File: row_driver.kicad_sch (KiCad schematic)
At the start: 26 parts, among them SW3 SW_PUSH_SMALL_H, SW4 SW_PUSH_SMALL_H, SW5 SW_PUSH_SMALL_H, SW6 SW_PUSH_SMALL_H, SW7 SW_PUSH_SMALL_H, SW8 SW_PUSH_SMALL_H, U11 74HCT595, U13 74HCT595, U15 74HCT595, U23 CM1293A-04SO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

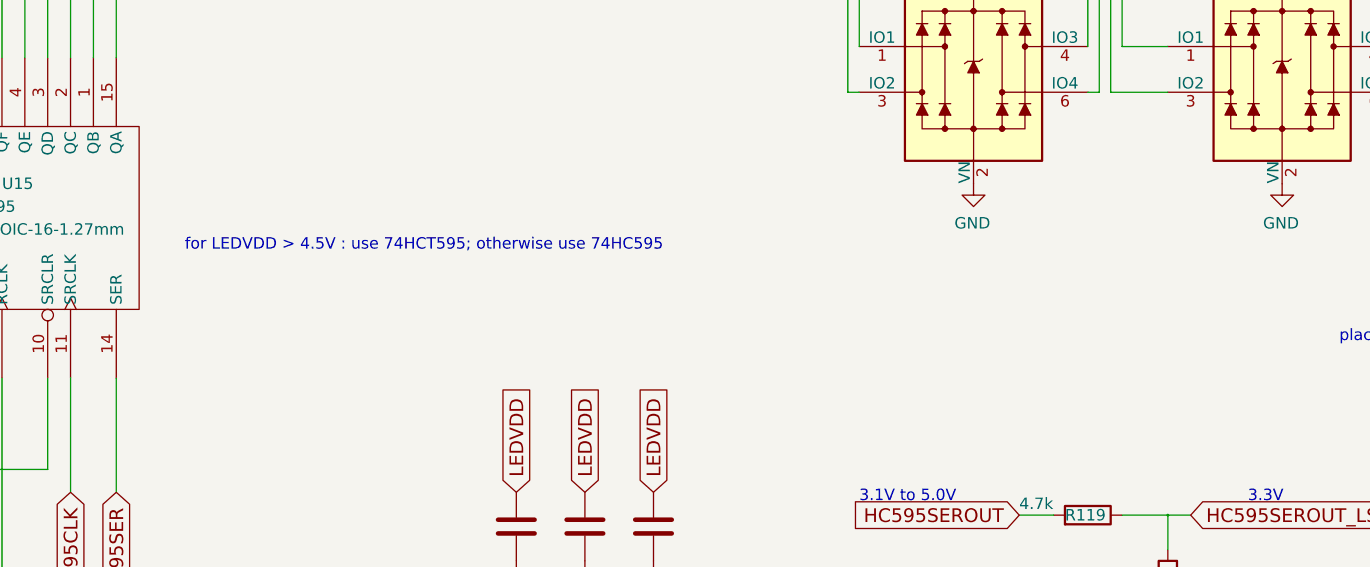
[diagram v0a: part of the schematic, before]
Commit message: Fixed bypass capacitor positions; DRC clear
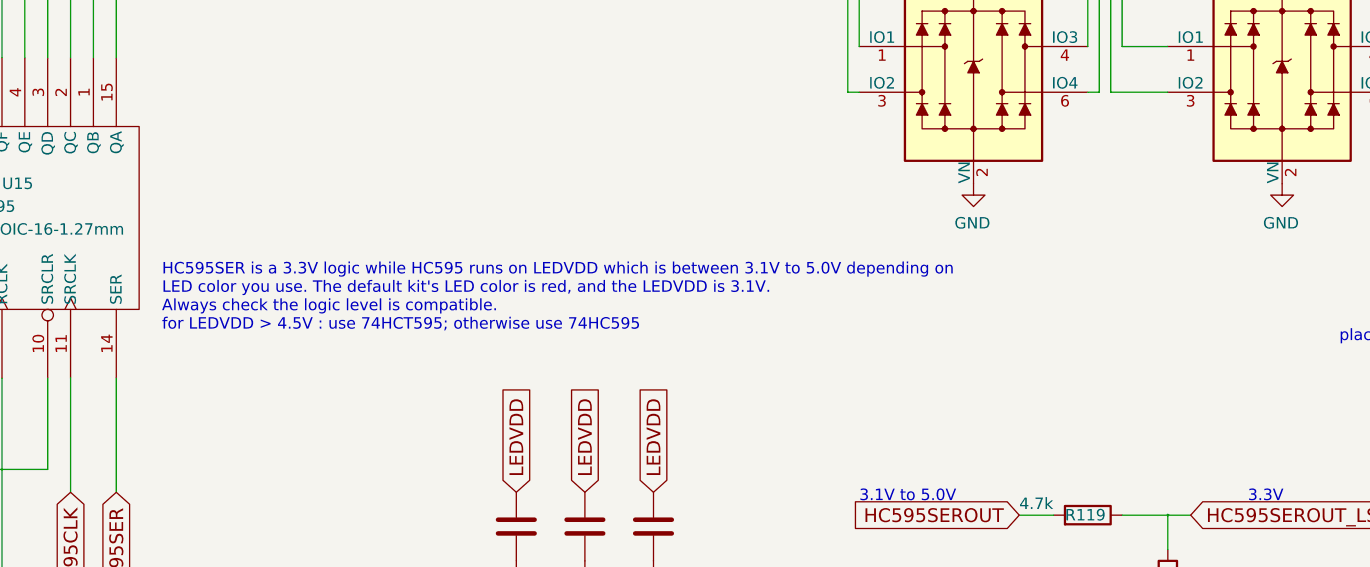
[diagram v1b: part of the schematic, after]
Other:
- note added: "HC595SER is a 3.3V logic while HC595 runs on LEDVDD which is between 3.1V to 5.0V depending on LED color you use. The default kit's LED color is red, and the LEDVDD is 3.1V. Always check the logic level is compatible. for LEDVDD > 4.5V : use 74HCT595; otherwise use 74HC595"
- note removed: "for LEDVDD > 4.5V : use 74HCT595; otherwise use 74HC595"
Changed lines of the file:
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@@
-(kicad_sch (version 20200820) (host eeschema "5.99.0-unknown-dd374e12a~102~ubuntu18.04.1")
+(kicad_sch (version 20200820) (host eeschema "5.99.0-unknown-b0af66afc~103~ubuntu18.04.1")
   (page 4 10)
   (paper "A4")
@@
     (stroke (width 0) (type solid) (color 0 0 0 0))
   )
-  (text "for LEDVDD > 4.5V : use 74HCT595; otherwise use 74HC595"
-    (at 132.08 99.06 0)
+  (text "HC595SER is a 3.3V logic while HC595 runs on LEDVDD which is between 3.1V to 5.0V depending on\nLED color you use. The default kit's LED color is red, and the LEDVDD is 3.1V.\nAlways check the logic level is compatible.\nfor LEDVDD > 4.5V : use 74HCT595; otherwise use 74HC595"
+    (at 129.54 107.95 0)
     (effects (font (size 1.27 1.27)) (justify left bottom))
   )

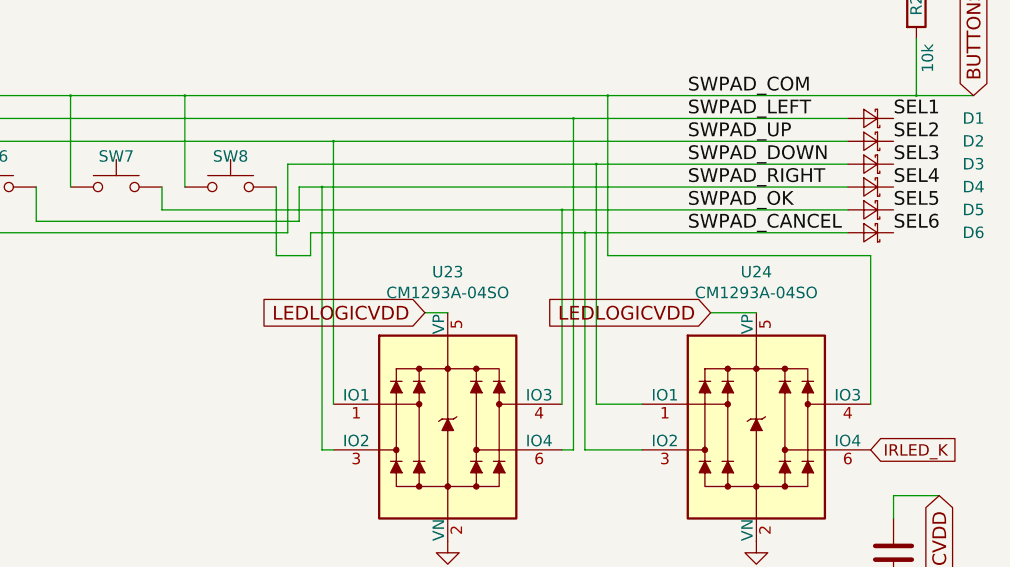
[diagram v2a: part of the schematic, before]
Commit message: Re-arranged physical buttions; DRC clear
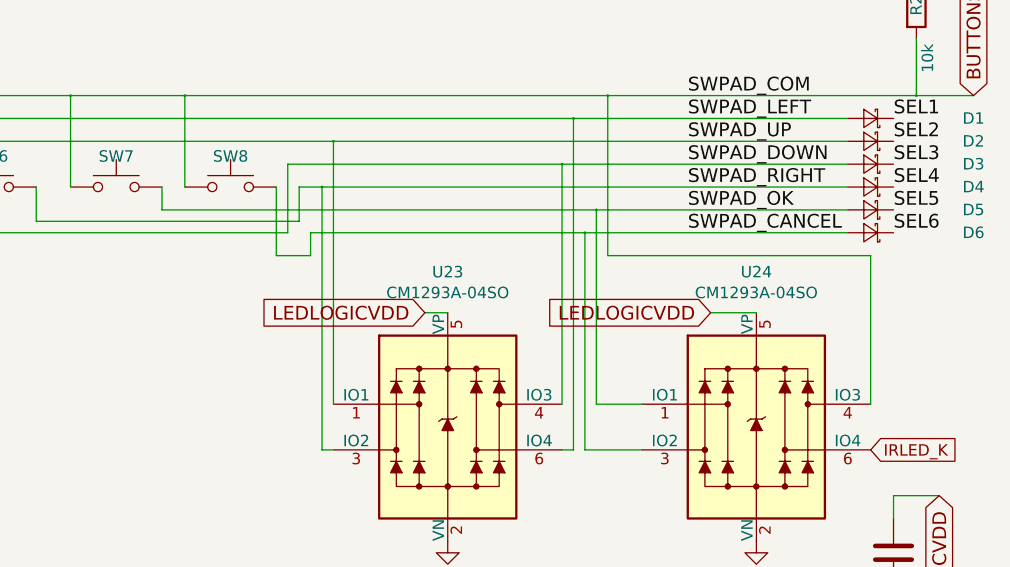
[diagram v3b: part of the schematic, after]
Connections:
- net SWPAD_DOWN: now also U23.4 (IO3); no longer U24.1 (IO1)
- net SWPAD_OK: now also U24.1 (IO1); no longer U23.4 (IO3)
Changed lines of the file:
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@@
-(kicad_sch (version 20200827) (generator eeschema)
+(kicad_sch (version 20200828) (generator eeschema)
   (page 4 10)
   (paper "A4")
@@
   (junction (at 205.74 52.07) (diameter 0.3048) (color 0 0 0 0))
   (junction (at 207.01 46.99) (diameter 0.3048) (color 0 0 0 0))
-  (junction (at 232.41 54.61) (diameter 0.3048) (color 0 0 0 0))
+  (junction (at 232.41 49.53) (diameter 0.3048) (color 0 0 0 0))
   (junction (at 233.68 44.45) (diameter 0.3048) (color 0 0 0 0))
   (junction (at 234.95 57.15) (diameter 0.3048) (color 0 0 0 0))
-  (junction (at 236.22 49.53) (diameter 0.3048) (color 0 0 0 0))
+  (junction (at 236.22 54.61) (diameter 0.3048) (color 0 0 0 0))
   (junction (at 237.49 41.91) (diameter 0.3048) (color 0 0 0 0))
   (junction (at 241.3 128.27) (diameter 0.3048) (color 0 0 0 0))
@@
     (stroke (width 0) (type solid) (color 0 0 0 0))
   )
-  (wire (pts (xy 187.96 54.61) (xy 232.41 54.61))
+  (wire (pts (xy 187.96 54.61) (xy 236.22 54.61))
     (stroke (width 0) (type solid) (color 0 0 0 0))
   )
@@
     (stroke (width 0) (type solid) (color 0 0 0 0))
   )
-  (wire (pts (xy 201.93 49.53) (xy 236.22 49.53))
+  (wire (pts (xy 201.93 49.53) (xy 232.41 49.53))
     (stroke (width 0) (type solid) (color 0 0 0 0))
   )
@@
     (stroke (width 0) (type solid) (color 0 0 0 0))
   )
-  (wire (pts (xy 232.41 54.61) (xy 232.41 76.2))
-    (stroke (width 0) (type solid) (color 0 0 0 0))
-  )
-  (wire (pts (xy 232.41 54.61) (xy 264.16 54.61))
+  (wire (pts (xy 232.41 49.53) (xy 232.41 76.2))
+    (stroke (width 0) (type solid) (color 0 0 0 0))
+  )
+  (wire (pts (xy 232.41 49.53) (xy 264.16 49.53))
     (stroke (width 0) (type solid) (color 0 0 0 0))
   )
@@
     (stroke (width 0) (type solid) (color 0 0 0 0))
   )
-  (wire (pts (xy 236.22 49.53) (xy 236.22 76.2))
-    (stroke (width 0) (type solid) (color 0 0 0 0))
-  )
-  (wire (pts (xy 236.22 49.53) (xy 264.16 49.53))
-    (stroke (width 0) (type solid) (color 0 0 0 0))
-  )
+  (wire (pts (xy 236.22 54.61) (xy 236.22 76.2))
+    (stroke (width 0) (type solid) (color 0 0 0 0))
+  )
+  (wire (pts (xy 236.22 54.61) (xy 264.16 54.61))
+    (stroke (width 0) (type solid) (color 0 0 0 0))
+  )

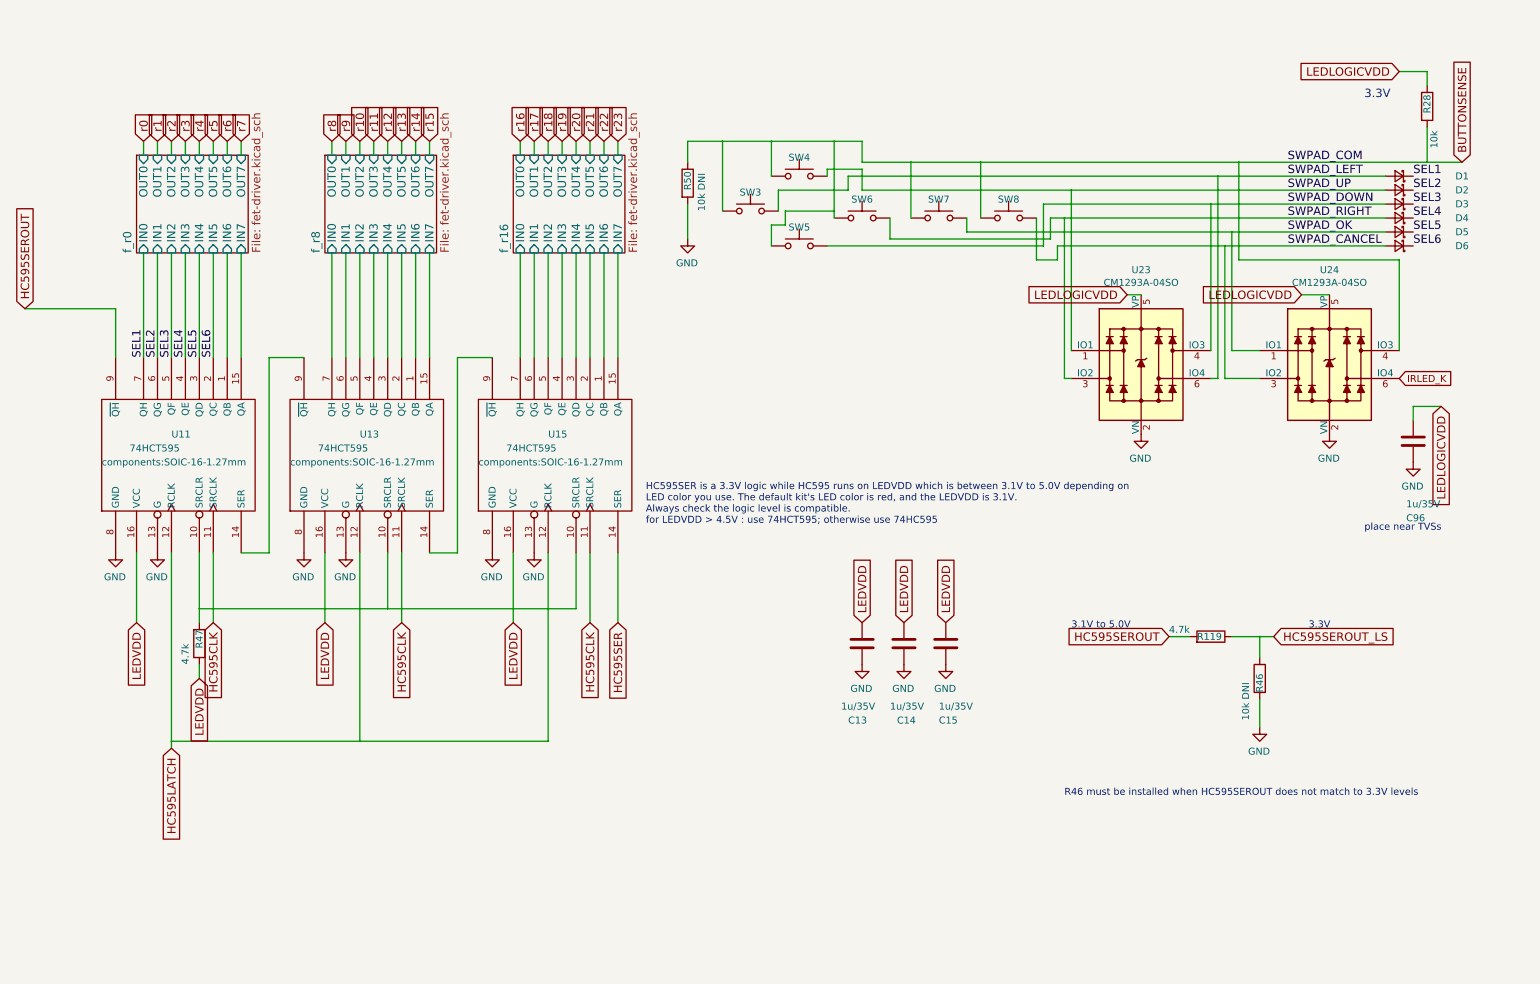
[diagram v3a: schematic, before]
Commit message: Use BAT54A instead of discrete Ds; DRC NOT clear
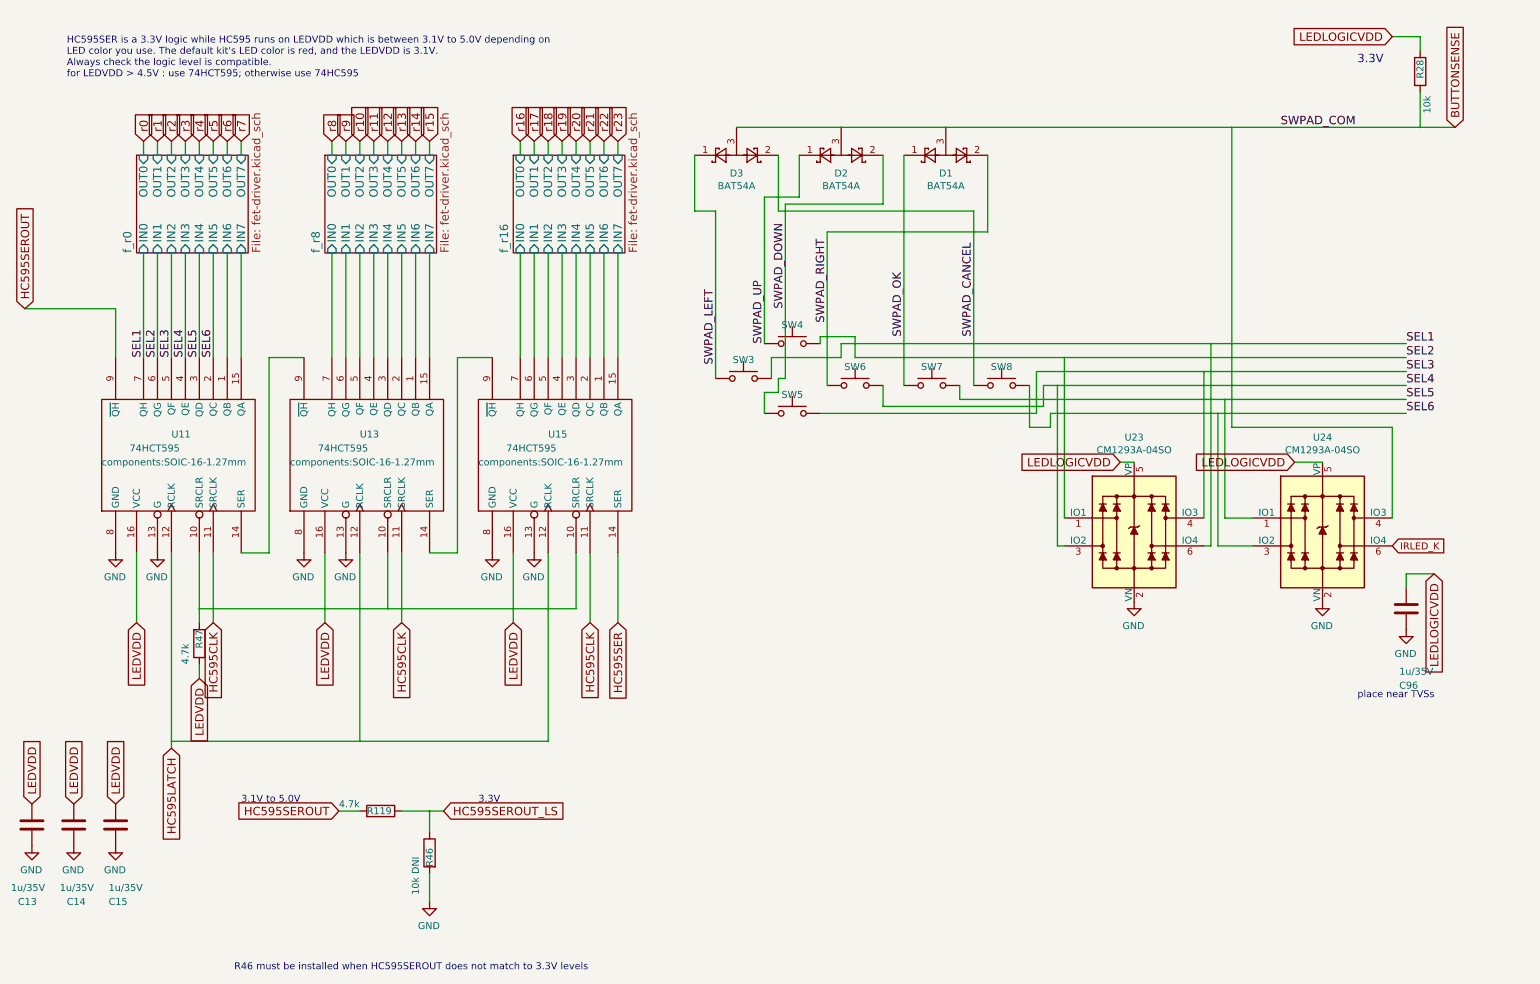
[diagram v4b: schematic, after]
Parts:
- removed D1, D2, D3, D4, D5, D6: D_Schottky_Small, components:SOD-523-mod, symbol dotmatrix_64x48-rescue:D_Schottky_Small-device
- removed R50: 10k DNI, Resistor_SMD:R_0603_1608Metric_Pad1.05x0.95mm_HandSolder, symbol dotmatrix_64x48-rescue:R-device
- added D1, D2, D3: BAT54A, Package_TO_SOT_SMD:SOT-23_Handsoldering, symbol Diode:BAT54A
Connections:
- net BUTTONSENSE: now also D1.3, D2.3, D3.3; no longer SW3.2, SW4.2, SW5.2, SW6.2, SW7.2, SW8.2
- net SEL1: now also SW3.1, U23.6 (IO4)
- net SEL2: now also SW4.1, U23.1 (IO1)
- net SEL3: now also SW5.1, U23.4 (IO3)
- net SEL4: now also SW6.1, U23.3 (IO2)
- net SEL5: now also SW7.1, U24.1 (IO1)
- net SEL6: now also SW8.1, U24.3 (IO2)
- net SWPAD_CANCEL: now also SW8.2, D3.2; no longer SW8.1, U24.3 (IO2)
- net SWPAD_DOWN: now also SW5.2, D2.2; no longer SW5.1, U23.4 (IO3)
- net SWPAD_LEFT: now also SW3.2, D3.1; no longer SW3.1, U23.6 (IO4)
- net SWPAD_OK: now also SW7.2, D1.1; no longer SW7.1, U24.1 (IO1)
- net SWPAD_RIGHT: now also SW6.2, D1.2; no longer SW6.1, U23.3 (IO2)
- net SWPAD_UP: now also SW4.2, D2.1; no longer SW4.1, U23.1 (IO1)
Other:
- moved on the sheet: C13, C14, C15, C96, R119, R28, R46, SW3, SW4, SW5, SW6, SW7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

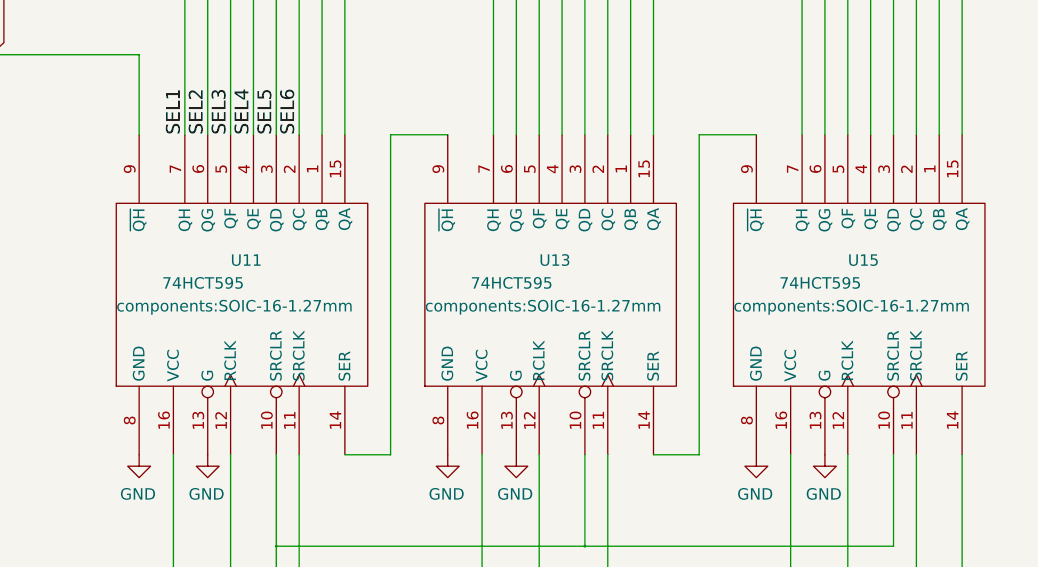
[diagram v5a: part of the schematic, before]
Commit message: Added a schematic comments; I don't know why other files are updated
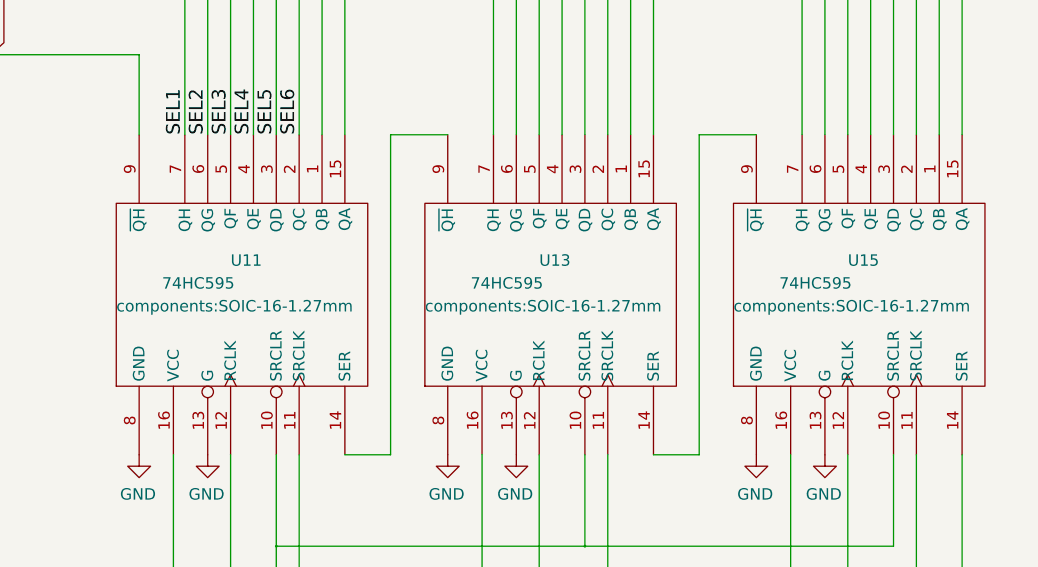
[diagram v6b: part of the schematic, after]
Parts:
- U11, U13, U15: value 74HCT595 -> 74HC595
